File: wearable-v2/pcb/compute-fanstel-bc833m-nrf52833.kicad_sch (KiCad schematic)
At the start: 19 parts, among them J5 EXT_1_SOCKET, U6 BC833, U7 MX25R8035FZxxx0, U8 PCF85063ATL, Y1 32.768kHz

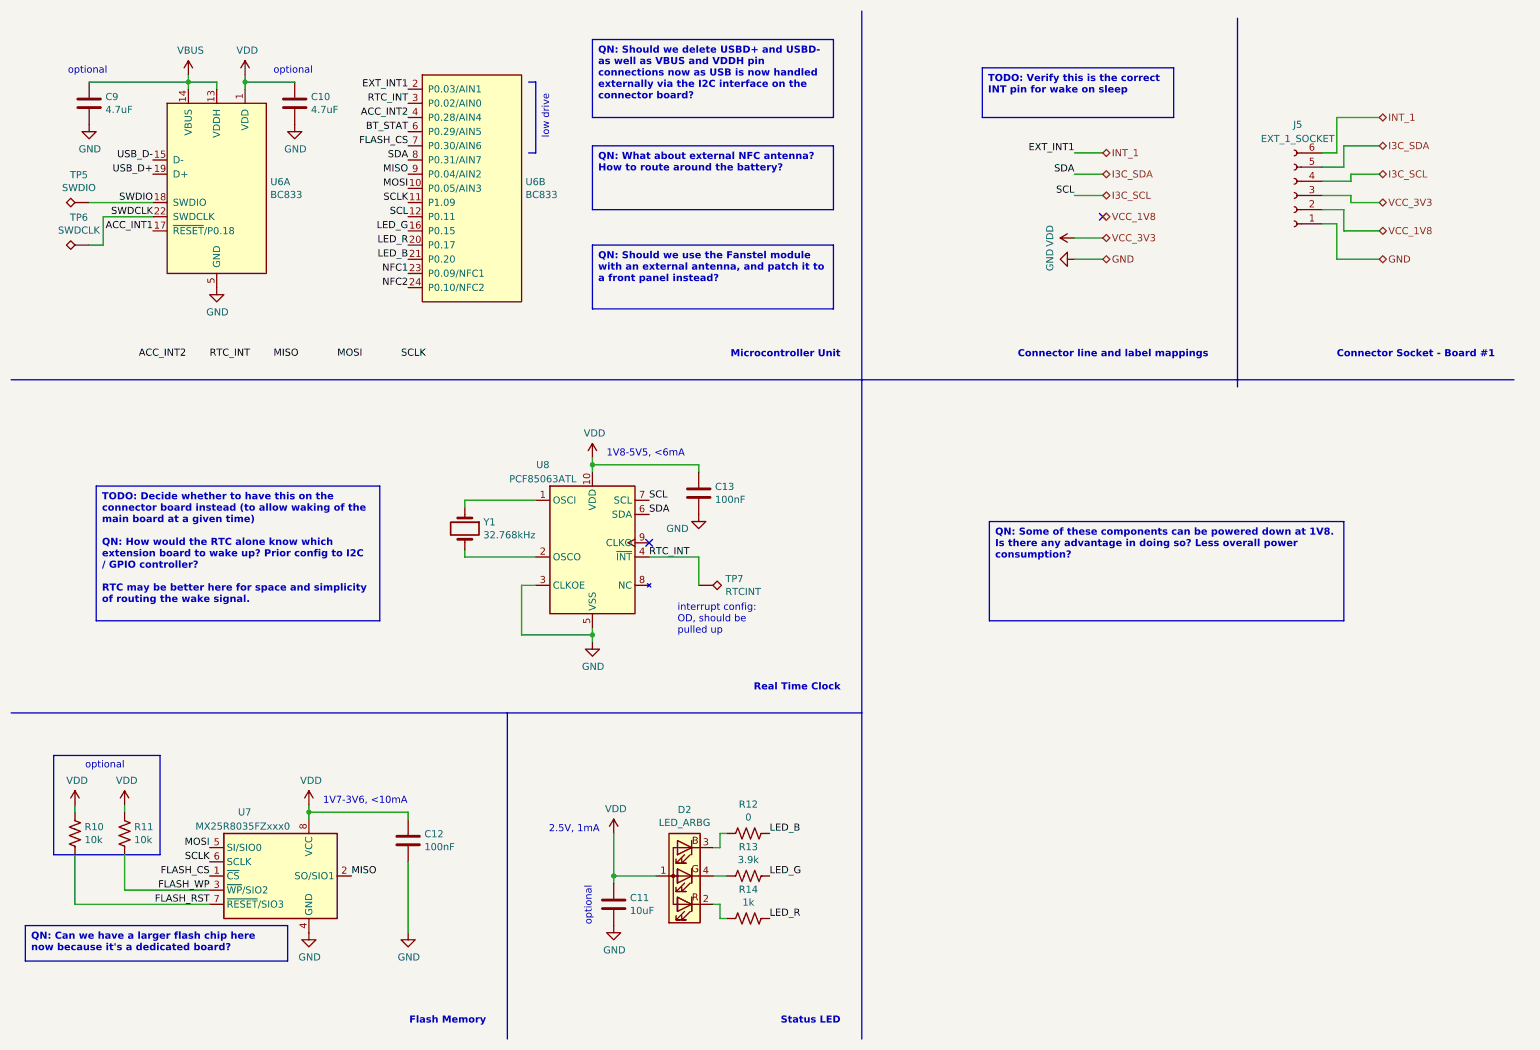
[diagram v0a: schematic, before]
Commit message: Updated components and PCB layout
Signed-off-by: Adam Fowler <adam@adamfowler.org>
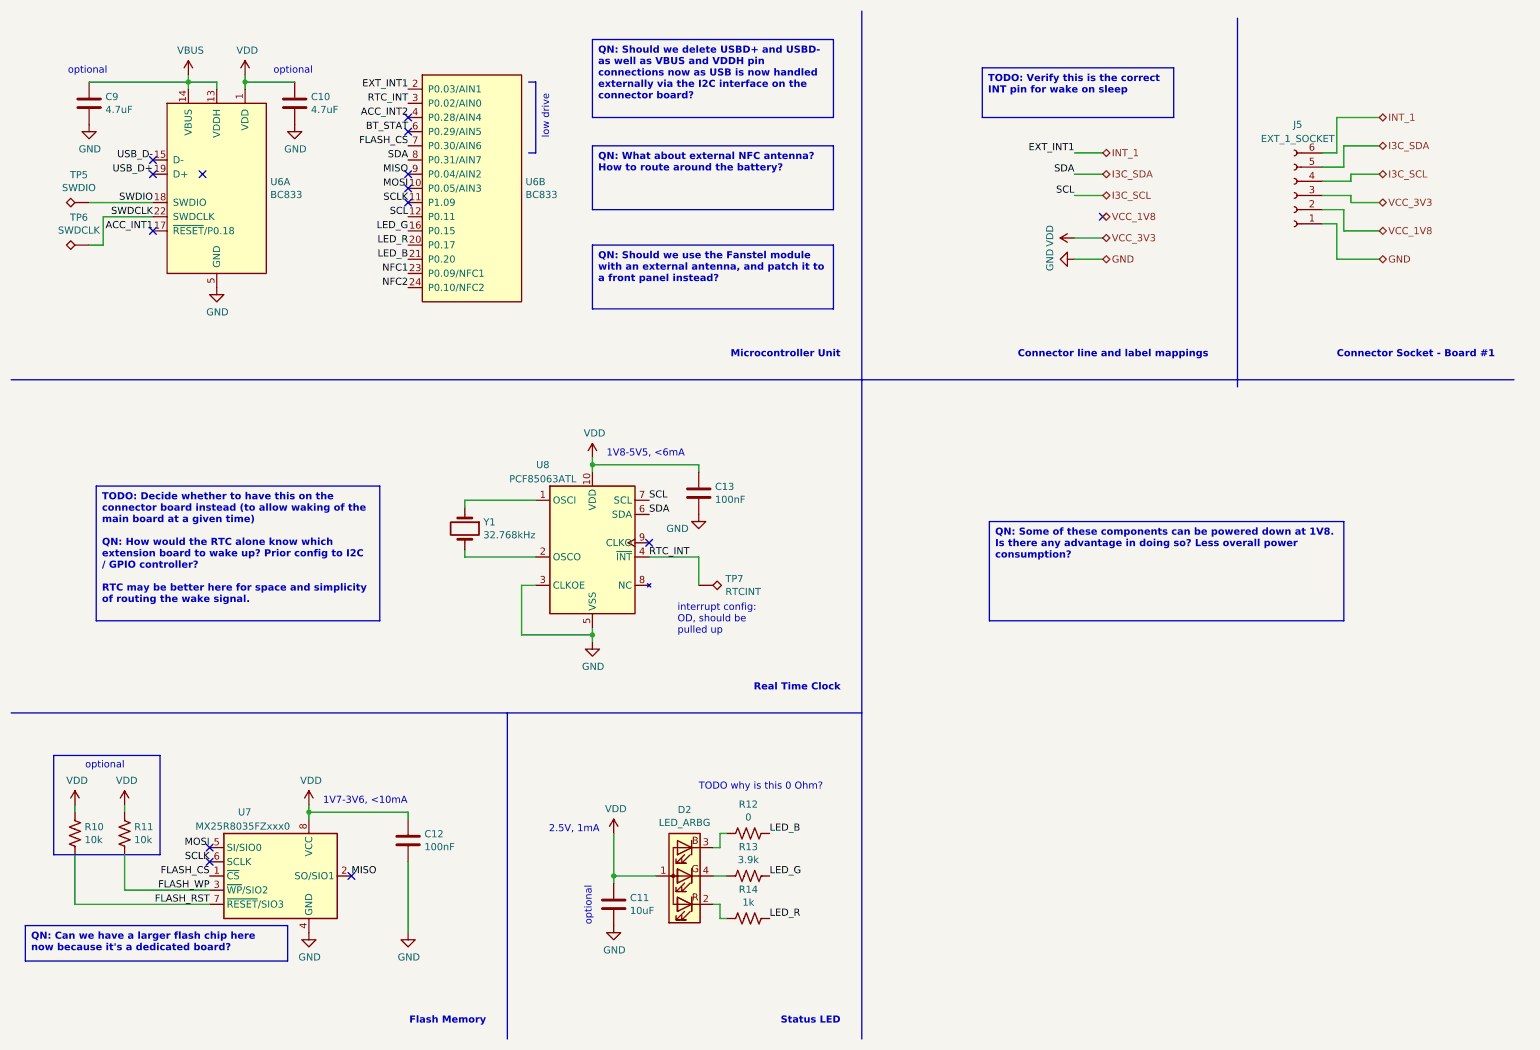
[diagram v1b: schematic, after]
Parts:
- D2: footprint Herald_Extras:LED_Kingbright_APHF1608 -> Herald:LED_Kingbright_APHF1608
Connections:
- no-connect marks 2 -> 14
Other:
- note added: "TODO why is this 0 Ohm?"
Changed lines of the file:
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@@
   (junction (at 118.11 93.98) (diameter 0) (color 0 0 0 0)
   )
+  (no_connect (at 39.37 52.07))
+  (no_connect (at 39.37 41.91))
+  (no_connect (at 39.37 39.37))
+  (no_connect (at 49.53 162.56))
+  (no_connect (at 49.53 165.1))
+  (no_connect (at 85.09 44.45))
+  (no_connect (at 85.09 41.91))
+  (no_connect (at 74.93 167.64))
   (no_connect (at 209.55 49.53))
   (no_connect (at 128.27 107.95))
+  (no_connect (at 85.09 46.99))
+  (no_connect (at 85.09 34.29))
+  (no_connect (at 85.09 31.75))
+  (no_connect (at 48.26 41.91))
   (wire (pts (xy 27.94 25.4) (xy 45.72 25.4))
     (stroke (width 0) (type default))
@@
     (effects (font (size 1.27 1.27) (thickness 0.254) bold) (justify left top))
   )
+  (text "TODO why is this 0 Ohm?" (at 137.16 152.4 0)
+    (effects (font (size 1.27 1.27)) (justify left bottom))
+  )
   (text "optional" (at 60.96 24.13 0)
     (effects (font (size 1.27 1.27)) (justify left bottom))
@@
     (effects (font (size 1.27 1.27)) (justify right bottom))
   )
-  (label "RTC_INT" (at 49.53 74.93 0) (fields_autoplaced)
-    (effects (font (size 1.27 1.27)) (justify left bottom))
-  )
-  (label "MISO" (at 60.96 74.93 0) (fields_autoplaced)
-    (effects (font (size 1.27 1.27)) (justify left bottom))
-  )
   (label "SCLK" (at 85.09 46.99 180) (fields_autoplaced)
     (effects (font (size 1.27 1.27)) (justify right bottom))
@@
     (effects (font (size 1.27 1.27)) (justify right bottom))
   )
-  (label "ACC_INT2" (at 36.83 74.93 0) (fields_autoplaced)
-    (effects (font (size 1.27 1.27)) (justify left bottom))
-  )
-  (label "MOSI" (at 72.39 74.93 0) (fields_autoplaced)
-    (effects (font (size 1.27 1.27)) (justify left bottom))
-  )
   (label "NFC2" (at 85.09 62.23 180) (fields_autoplaced)
     (effects (font (size 1.27 1.27)) (justify right bottom))
@@
   )
   (label "MISO" (at 74.93 167.64 0) (fields_autoplaced)
-    (effects (font (size 1.27 1.27)) (justify left bottom))
-  )
-  (label "SCLK" (at 83.82 74.93 0) (fields_autoplaced)
     (effects (font (size 1.27 1.27)) (justify left bottom))
   )
@@
       (effects (font (size 1.27 1.27)))
     )
-    (property "Footprint" "Herald_Extras:LED_Kingbright_APHF1608" (at 134.62 166.37 0)
-      (effects (font (size 1.27 1.27)) hide)
-    )
+    (property "Footprint" "Herald:LED_Kingbright_APHF1608" (at 134.62 166.37 0)
+      (effects (font (size 1.27 1.27)) hide)
+    )

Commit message: Further V2 routing
Signed-off-by: Adam Fowler <adam@adamfowler.org>
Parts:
- U6: footprint Herald_Extras:Fanstel_BC833x -> Herald:Fanstel_BC833x
- U7: footprint Herald_Extras:USON-8-1EP_2x3mm_P0.5mm_EP0.25x1.65mm -> Herald:USON-8-1EP_2x3mm_P0.5mm_EP0.25x1.65mm
- U8: footprint Herald_Extras:DFN-10-1EP_2.6x2.6mm_P0.5mm_EP1.25x2.15mm -> Herald:DFN-10-1EP_2.6x2.6mm_P0.5mm_EP1.25x2.15mm
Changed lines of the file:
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@@
       (effects (font (size 1.27 1.27)))
     )
-    (property "Footprint" "Herald_Extras:DFN-10-1EP_2.6x2.6mm_P0.5mm_EP1.25x2.15mm" (at 118.11 109.22 0)
+    (property "Footprint" "Herald:DFN-10-1EP_2.6x2.6mm_P0.5mm_EP1.25x2.15mm" (at 118.11 109.22 0)
       (effects (font (size 1.27 1.27)) hide)
     )
@@
       (effects (font (size 1.27 1.27)) (justify left))
     )
-    (property "Footprint" "Herald_Extras:Fanstel_BC833x" (at 35.56 34.29 0)
+    (property "Footprint" "Herald:Fanstel_BC833x" (at 35.56 34.29 0)
       (effects (font (size 1.27 1.27)) hide)
     )
@@
       (effects (font (size 1.27 1.27)) (justify left))
     )
-    (property "Footprint" "Herald_Extras:USON-8-1EP_2x3mm_P0.5mm_EP0.25x1.65mm" (at 62.23 182.88 0)
+    (property "Footprint" "Herald:USON-8-1EP_2x3mm_P0.5mm_EP0.25x1.65mm" (at 62.23 182.88 0)
       (effects (font (size 1.27 1.27)) hide)
     )
@@
       (effects (font (size 1.27 1.27)) (justify left))
     )
-    (property "Footprint" "Herald_Extras:Fanstel_BC833x" (at 81.28 34.29 0)
-      (effects (font (size 1.27 1.27)) hide)
-    )
+    (property "Footprint" "Herald:Fanstel_BC833x" (at 81.28 34.29 0)
+      (effects (font (size 1.27 1.27)) hide)
+    )

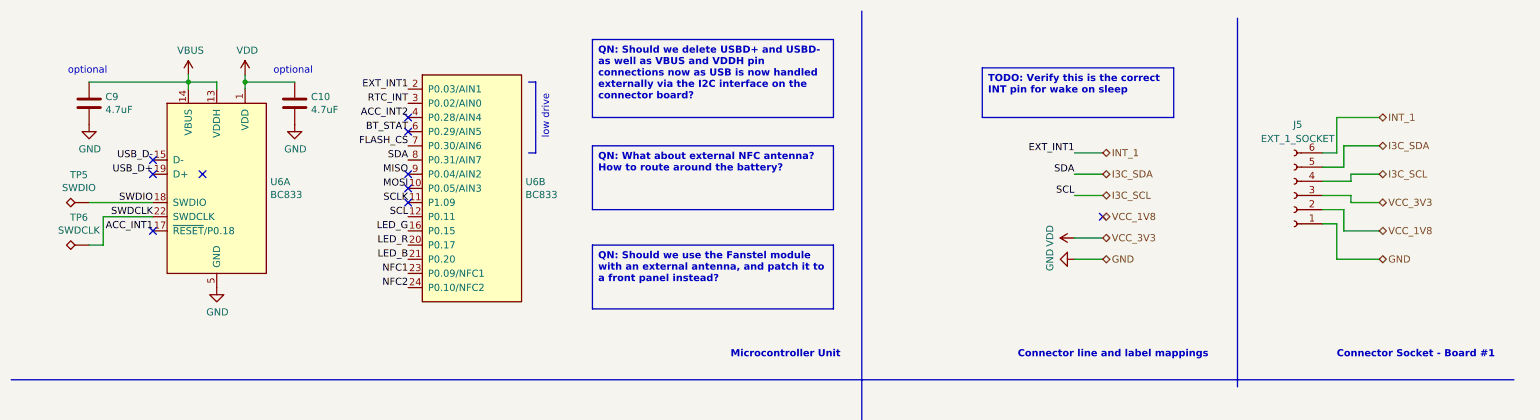
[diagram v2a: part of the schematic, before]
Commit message: Added front connectors on main board
Signed-off-by: Adam Fowler <adam@adamfowler.org>
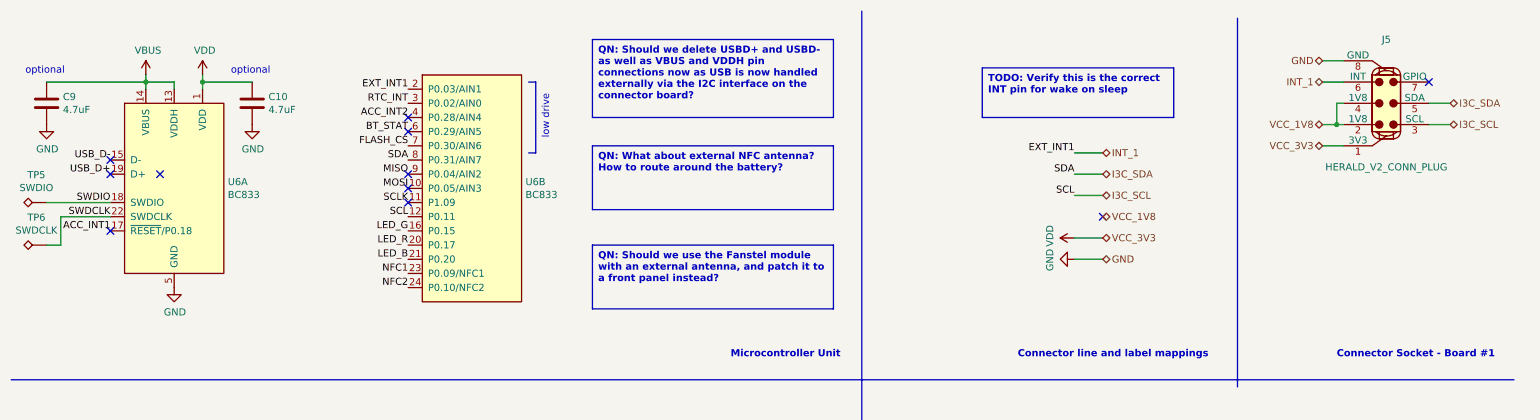
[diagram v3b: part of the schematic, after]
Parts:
- removed J5: EXT_1_SOCKET, symbol Connector:Conn_01x06_Socket
- added J5: HERALD_V2_CONN_PLUG, symbol Herald_Extras:HERALD_V2_CONN_PLUG
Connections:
- net GND: now also J5.8 (GND)
- net I3C_SCL: now also J5.3 (SCL)
- net I3C_SDA: now also J5.5 (SDA)
- net INT_1: now also J5.6 (INT)
- net VCC_1V8: now also J5.2 (1V8), J5.4 (1V8)
- net VDD: now also J5.1 (3V3)
- no-connect marks 14 -> 15
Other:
- moved on the sheet: C10, C9, TP5, TP6, U6A

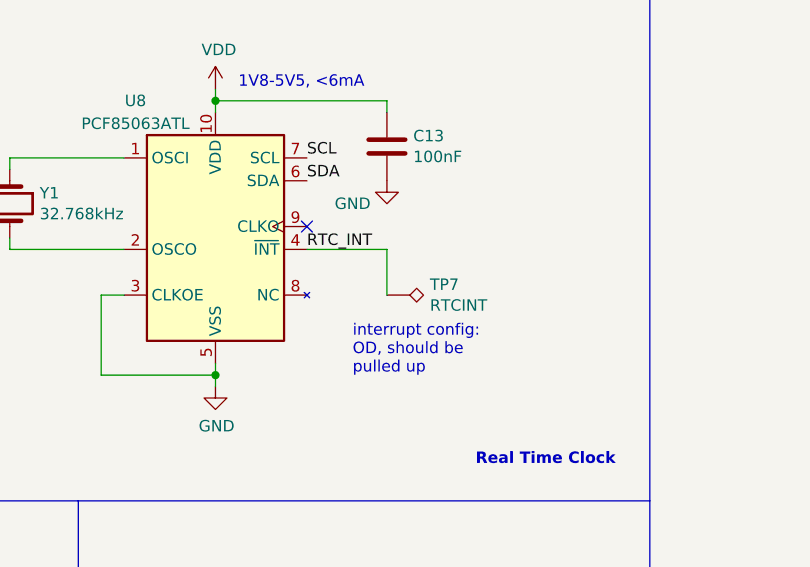
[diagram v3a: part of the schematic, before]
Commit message: Set wider PCB GND tracks and vias
Signed-off-by: Adam Fowler <adam@adamfowler.org>
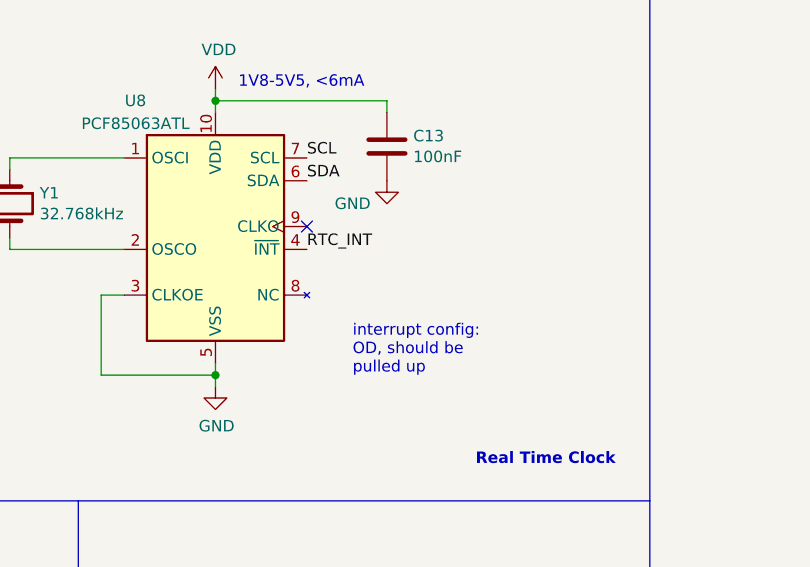
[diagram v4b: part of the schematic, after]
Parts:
- removed TP7: RTCINT, TestPoint:TestPoint_Pad_D1.0mm, symbol Connector:TestPoint_Alt
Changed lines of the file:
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@@
-    (stroke (width 0) (type default))
-  )
-  (wire (pts (xy 137.16 110.49) (xy 137.16 115.57))
     (stroke (width 0) (type default))
   )
@@
   )
   (wire (pts (xy 85.09 156.21) (xy 85.09 157.48))
-    (stroke (width 0) (type default))
-  )
-  (wire (pts (xy 137.16 110.49) (xy 128.27 110.49))
     (stroke (width 0) (type default))
   )
@@
         )
       )
-    )
-  )
-  (symbol (lib_id "Connector:TestPoint_Alt") (at 137.16 115.57 270) (unit 1)
-    (in_bom yes) (on_board yes) (dnp no)
-    (property "Reference" "TP7" (at 141.9352 114.4016 90)
-      (effects (font (size 1.27 1.27)) (justify left))
-    )
-    (property "Value" "RTCINT" (at 141.9352 116.713 90)
-      (effects (font (size 1.27 1.27)) (justify left))
-    )
-    (property "Footprint" "TestPoint:TestPoint_Pad_D1.0mm" (at 137.16 120.65 0)
-      (effects (font (size 1.27 1.27)) hide)
-    )
-    (property "Datasheet" "~" (at 137.16 120.65 0)
-      (effects (font (size 1.27 1.27)) hide)
-    )
-    (property "Description" "Test point" (at 137.16 115.57 0)
-      (effects (font (size 1.27 1.27)) hide)
-    )
-    (property "MPN" "~" (at 137.16 115.57 0)
-      (effects (font (size 1.27 1.27)) hide)
-    )
-    (pin "1")
-    (instances
-      (project "wearable-v2"
-        (path "/1eb7e8c9-86dc-4f6b-85aa-748b782af952/88c842d7-ac9a-4ec4-bd18-165411775e80"
-          (reference "TP7") (unit 1)
-        )
-      )
-      (project "wearable"
-        (path "/bdd943b2-035a-4beb-80ad-5c7e84260dde/00000000-0000-0000-0000-000060f1d377"
-          (reference "TP72") (unit 1)
-        )
-      )

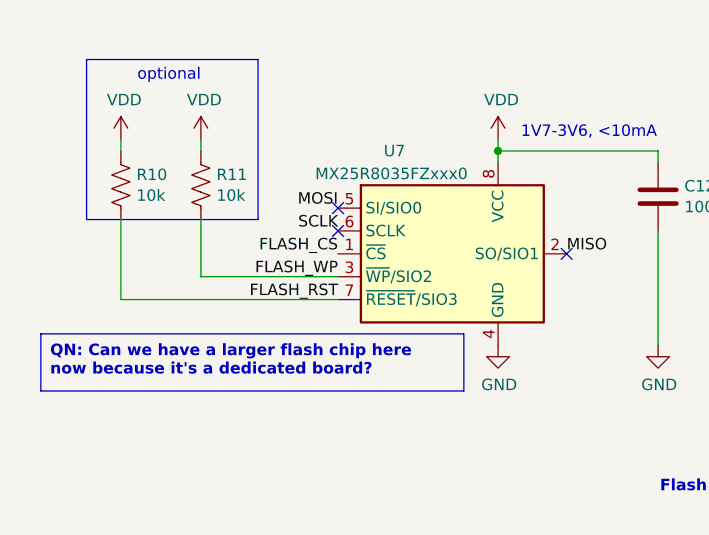
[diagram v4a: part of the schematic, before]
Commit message: Upgraded flash and corrected XIF placement
Signed-off-by: Adam Fowler <adam@adamfowler.org>
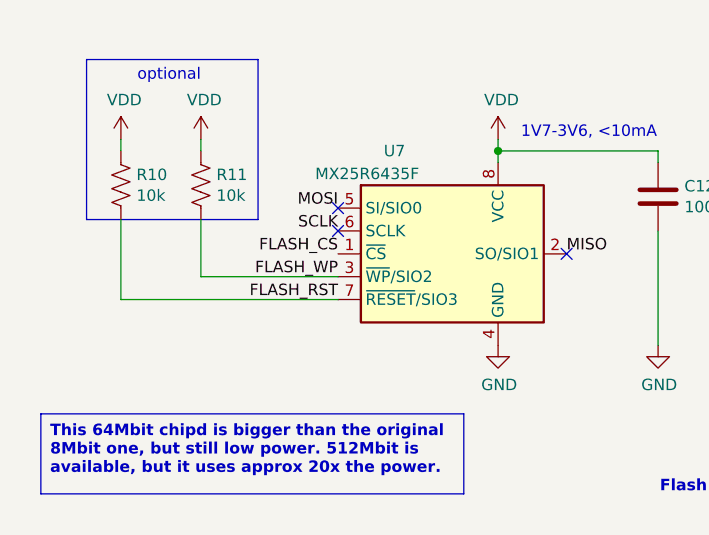
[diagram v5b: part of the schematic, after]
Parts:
- U7: value MX25R8035FZxxx0 -> MX25R6435F; footprint Herald:USON-8-1EP_2x3mm_P0.5mm_EP0.25x1.65mm -> Package_SON:WSON-8-1EP_6x5mm_P1.27mm_EP3.4x4mm; MPN MX25R8035FZUIL0 -> MX25R6435FZNIL0
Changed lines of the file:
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@@
     (effects (font (size 1.27 1.27) (thickness 0.254) bold) (justify left top))
   )
-  (text_box "QN: Can we have a larger flash chip here now because it's a dedicated board?"
-    (at 16.51 176.53 0) (size 46.99 6.35)
+  (text_box "This 64Mbit chipd is bigger than the original 8Mbit one, but still low power. 512Mbit is available, but it uses approx 20x the power."
+    (at 16.51 185.42 0) (size 46.99 8.89)
     (stroke (width 0) (type default))
     (fill (type none))
@@
       (effects (font (size 1.27 1.27)) (justify left))
     )
-    (property "Value" "MX25R8035FZxxx0" (at 46.99 158.75 0)
-      (effects (font (size 1.27 1.27)) (justify left))
-    )
-    (property "Footprint" "Herald:USON-8-1EP_2x3mm_P0.5mm_EP0.25x1.65mm" (at 62.23 182.88 0)
-      (effects (font (size 1.27 1.27)) hide)
-    )
-    (property "Datasheet" "https://www.macronix.com/Lists/Datasheet/Attachments/7934/MX25R8035F,%20Wide%20Range,%208Mb,%20v1.6.pdf" (at 62.23 167.64 0)
-      (effects (font (size 1.27 1.27)) hide)
-    )
-    (property "Description" "Flash memory, SPI" (at 62.23 167.64 0)
-      (effects (font (size 1.27 1.27)) hide)
-    )
-    (property "MPN" "MX25R8035FZUIL0" (at 62.23 167.64 0)
-      (effects (font (size 1.27 1.27)) hide)
-    )
+    (property "Value" "MX25R6435F" (at 46.99 158.75 0)
+      (effects (font (size 1.27 1.27)) (justify left))
+    )
+    (property "Footprint" "Package_SON:WSON-8-1EP_6x5mm_P1.27mm_EP3.4x4mm" (at 62.23 182.88 0)
+      (effects (font (size 1.27 1.27)) hide)
+    )
+    (property "Datasheet" "https://www.macronix.com/Lists/Datasheet/Attachments/8868/MX25R6435F,%20Wide%20Range,%2064Mb,%20v1.6.pdf" (at 62.23 167.64 0)
+      (effects (font (size 1.27 1.27)) hide)
+    )
+    (property "Description" "Flash memory, SPI, 64Mbit" (at 62.23 167.64 0)
+      (effects (font (size 1.27 1.27)) hide)
+    )
+    (property "MPN" "MX25R6435FZNIL0" (at 62.23 167.64 0)
+      (effects (font (size 1.27 1.27)) hide)
+    )
